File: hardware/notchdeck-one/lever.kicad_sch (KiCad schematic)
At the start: 5 parts, among them U5 AS5600

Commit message: Add schematic wiring notes support
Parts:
- added C14, C15, C16, C17: 100nF, Capacitor_SMD:C_0402_1005Metric, symbol Device:C
- added J5: CODE S0, Connector_JST:JST_PH_S2B-PH-SM4-TB_1x02-1MP_P2.00mm_Horizontal, symbol Connector_Generic:Conn_01x02
- added J6: CODE S1, Connector_JST:JST_PH_S2B-PH-SM4-TB_1x02-1MP_P2.00mm_Horizontal, symbol Connector_Generic:Conn_01x02
- added J7: CODE S2, Connector_JST:JST_PH_S2B-PH-SM4-TB_1x02-1MP_P2.00mm_Horizontal, symbol Connector_Generic:Conn_01x02
- added J8: CODE S3, Connector_JST:JST_PH_S2B-PH-SM4-TB_1x02-1MP_P2.00mm_Horizontal, symbol Connector_Generic:Conn_01x02
- added R14, R15, R16, R17: 10k, Resistor_SMD:R_0402_1005Metric, symbol Device:R
- added R18, R19, R20, R21: 1k, Resistor_SMD:R_0402_1005Metric, symbol Device:R
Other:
- note added: "NotchDeck One — Lever sensing: AS5600 magnetic angle (I2C0) + 4-bit coded-switch input (J5). Placed, not wired. See NETPLAN.md "Lever sensing". AS5600 U5: VDD5V(1) + VDD3V3(2) -> +3V3 (3.3V mode: tie both). GND(4) -> GND. DIR(8) -> GND (CW = increasing). SDA(6) / SCL(7) -> I2C0 bus. OUT(3) = NC, PGO(5) = NC. C11 100nF + C12 1uF decouple. I2C0 (TWIM0): SDA = P0.26 (pad 12), SCL = P0.06 (pad 14). R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"
- note removed: "NotchDeck One — Lever sensor (U5 AS5600, magnetic angle). Placed, not wired. See NETPLAN.md "I2C buses" / "Lever sensing". AS5600 U5: VDD5V(1) + VDD3V3(2) -> +3V3 (3.3V mode: tie both). GND(4) -> GND. DIR(8) -> GND (CW = increasing). SDA(6) / SCL(7) -> I2C0 bus. OUT(3) = NC, PGO(5) = NC. C11 100nF + C12 1uF decouple. I2C0 (TWIM0): SDA = P0.26 (pad 12), SCL = P0.06 (pad 14). R9 / R10 = 4.7k pull-u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"
- title: NotchDeck One — Lever sensor (AS5600, I2C0) -> NotchDeck One — Lever sensing (AS5600 magnetic + 4-bit coded-switch)

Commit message: Wire and verify NotchDeck controller schematics
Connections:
- net at R19.1: now also J6.1 (Pin_1), R15.2
- net LEVER_S1: now reaches R19.2
- net LEVER_S1: now also C15.1
- net +3V3: now reaches R9.1
- net +3V3: now also C11.1, C12.1, R10.1, R14.1, R15.1, R16.1, R17.1, U5.1 (VDD5V), U5.2 (VDD3V3)
- net I2C0_SDA: now reaches R9.2
- net I2C0_SDA: now also U5.6 (SDA)
- net LEVER_S0: now reaches C14.1
- net LEVER_S0: now also R18.2
- net GND: now reaches C14.2
- net GND: now also C11.2, C12.2, C15.2, C16.2, C17.2, J5.2 (Pin_2), J6.2 (Pin_2), J7.2 (Pin_2), J8.2 (Pin_2), U5.4 (GND), U5.8 (DIR)
- net LEVER_S3: now reaches C17.1
- net LEVER_S3: now also R21.2
- net at J5.1 (Pin_1): now also R14.2, R18.1
- net at J8.1 (Pin_1): now also R17.2, R21.1
- net I2C0_SCL: now reaches U5.7 (SCL)
- net I2C0_SCL: now also R10.2
- net at J7.1 (Pin_1): now also R16.2, R20.1
- net LEVER_S2: now reaches C16.1
- net LEVER_S2: now also R20.2
- no-connect marks 0 -> 2
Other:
- note added: "AS5600: 3.3V mode, VDD5V tied to VDD3V3. I2C0 / 0x36; separate from the fuel gauge. DIR = GND, clockwise increases angle. OUT and PGO intentionally unused."
- note added: "J5-J8: pin 1 = switch signal, pin 2 = GND. Both sensing front-ends may be populated. RC release ~1.1ms, press ~0.1ms. Firmware still debounces and decodes binary/Gray detent codes."
- note added: "S0: switch closes to GND. 10k pull-up / 1k series / 100nF."
- note added: "S1: switch closes to GND. 10k pull-up / 1k series / 100nF."
- note added: "S2: switch closes to GND. 10k pull-up / 1k series / 100nF."
- note added: "S3: switch closes to GND. 10k pull-up / 1k series / 100nF."
- note removed: "NotchDeck One — Lever sensing: AS5600 magnetic angle (I2C0) + 4-bit coded-switch input (J5). Placed, not wired. See NETPLAN.md "Lever sensing". AS5600 U5: VDD5V(1) + VDD3V3(2) -> +3V3 (3.3V mode: tie both). GND(4) -> GND. DIR(8) -> GND (CW = increasing). SDA(6) / SCL(7) -> I2C0 bus. OUT(3) = NC, PGO(5) = NC. C11 100nF + C12 1uF decouple. I2C0 (TWIM0): SDA = P0.26 (pad 12), SCL = P0.06 (pad 14). R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"
- title: NotchDeck One — Lever sensing (AS5600 magnetic + 4-bit coded-switch) -> NotchDeck One — Lever sensing

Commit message: Source controller BOM from JLCPCB and align selected footprints
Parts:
- C11, C14, C15, C16, C17: BOM Checked (none) -> 2026-10-03; BOM Comments (none) -> 100nF 16V X7R ±10% 0402 Multilayer Ceramic Capacitors MLCC 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; JLCPCB Part Type (none) -> Basic; LCSC (none) -> C1525; MPN (none) -> CL05B104KO5NNNC; Manufacturer (none) -> Samsung Electro-Mechanics
- C12: BOM Checked (none) -> 2026-10-03; BOM Comments (none) -> 1uF 25V X5R ±10% 0402 Multilayer Ceramic Capacitors MLCC - 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; JLCPCB Part Type (none) -> Basic; LCSC (none) -> C52923; MPN (none) -> CL05A105KA5NQNC; Manufacturer (none) -> Samsung Electro-Mechanics
- J5, J6, J7, J8: BOM Checked (none) -> 2026-10-03; BOM Comments (none) -> Mating harnesses not included. J2: protected 1S cell, pin 1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; JLCPCB Part Type (none) -> Extended; LCSC (none) -> C295747; MPN S2B-PH-SM4-TB -> S2B-PH-SM4-TB(LF)(SN)
- R10, R9: BOM Checked (none) -> 2026-10-03; BOM Comments (none) -> -55℃~+155℃ 4.7kΩ 50V 62.5mW Thick Film Resistor ±1% ±100ppm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; JLCPCB Part Type (none) -> Basic; LCSC (none) -> C25900; MPN (none) -> 0402WGF4701TCE; Manufacturer (none) -> UNI-ROYAL
- R14, R15, R16, R17: BOM Checked (none) -> 2026-10-03; BOM Comments (none) -> -55℃~+155℃ 10kΩ 50V 62.5mW Thick Film Resistor ±1% ±100ppm/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; JLCPCB Part Type (none) -> Basic; LCSC (none) -> C25744; MPN (none) -> 0402WGF1002TCE; Manufacturer (none) -> UNI-ROYAL
- R18, R19, R20, R21: BOM Checked (none) -> 2026-10-03; BOM Comments (none) -> -55℃~+155℃ 1kΩ 50V 62.5mW Thick Film Resistor ±1% ±100ppm/℃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; JLCPCB Part Type (none) -> Basic; LCSC (none) -> C11702; MPN (none) -> 0402WGF1001TCE; Manufacturer (none) -> UNI-ROYAL
- U5: BOM Checked (none) -> 2026-10-03; JLCPCB Part Type (none) -> Extended; MPN AS5600-ASOM -> AS5600-ASOT; Manufacturer AMS -> ams

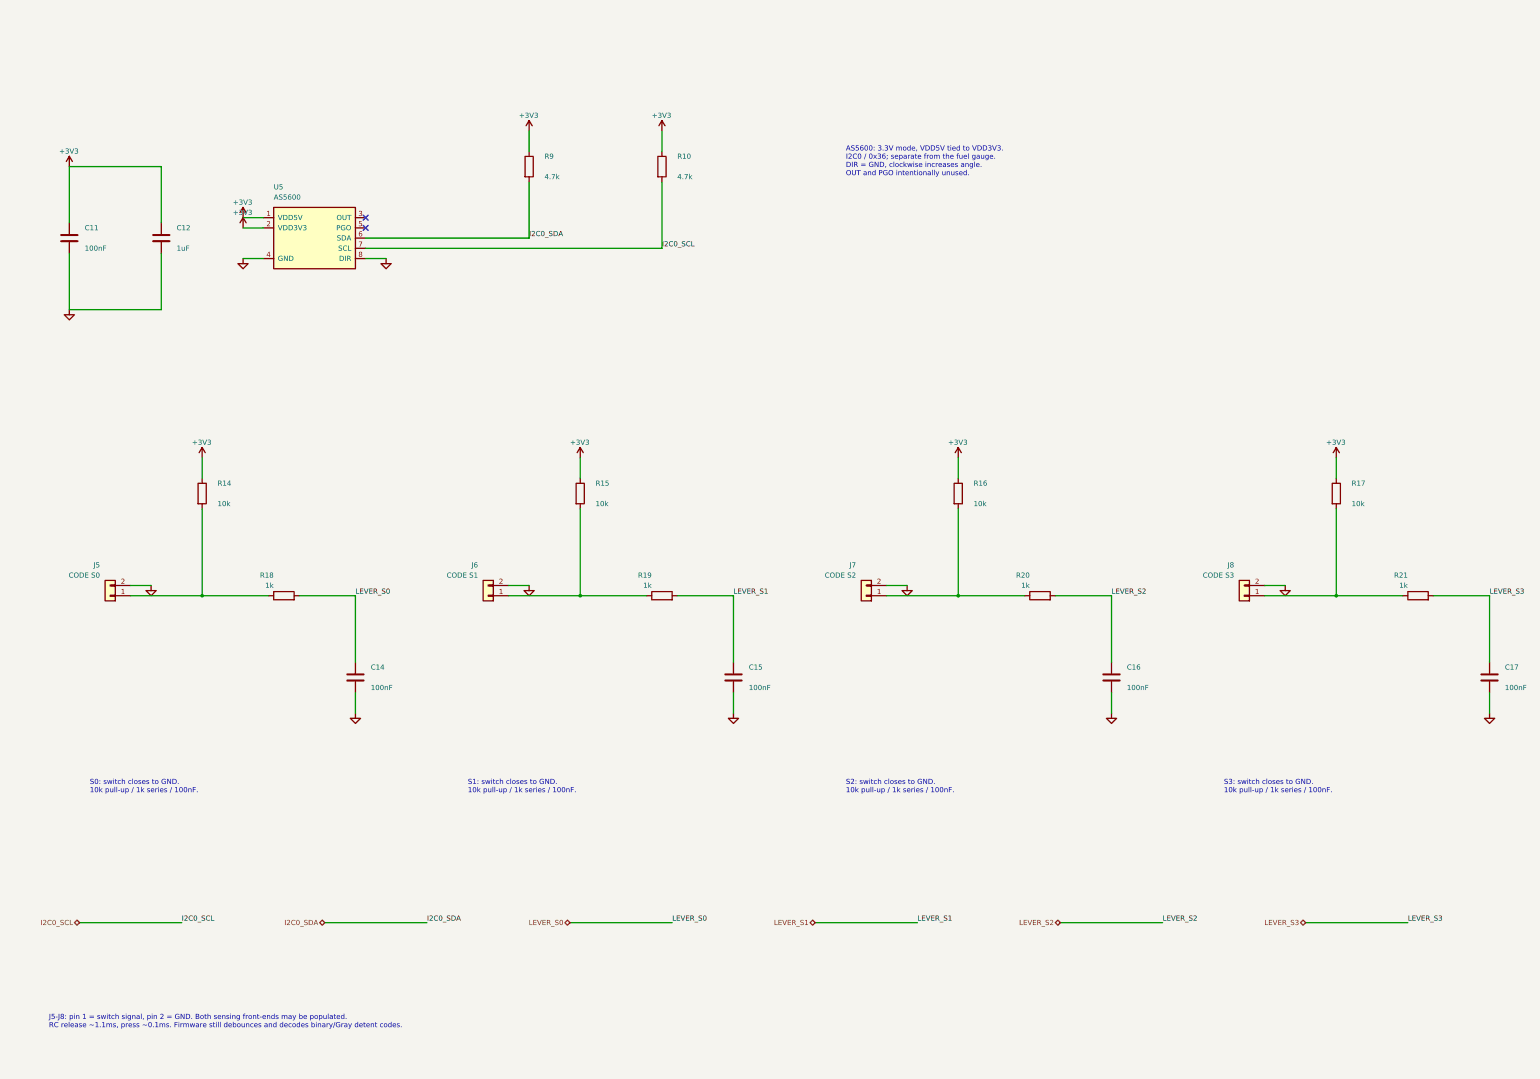
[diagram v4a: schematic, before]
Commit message: Support independent magnetic and Gray-coded power and brake handles
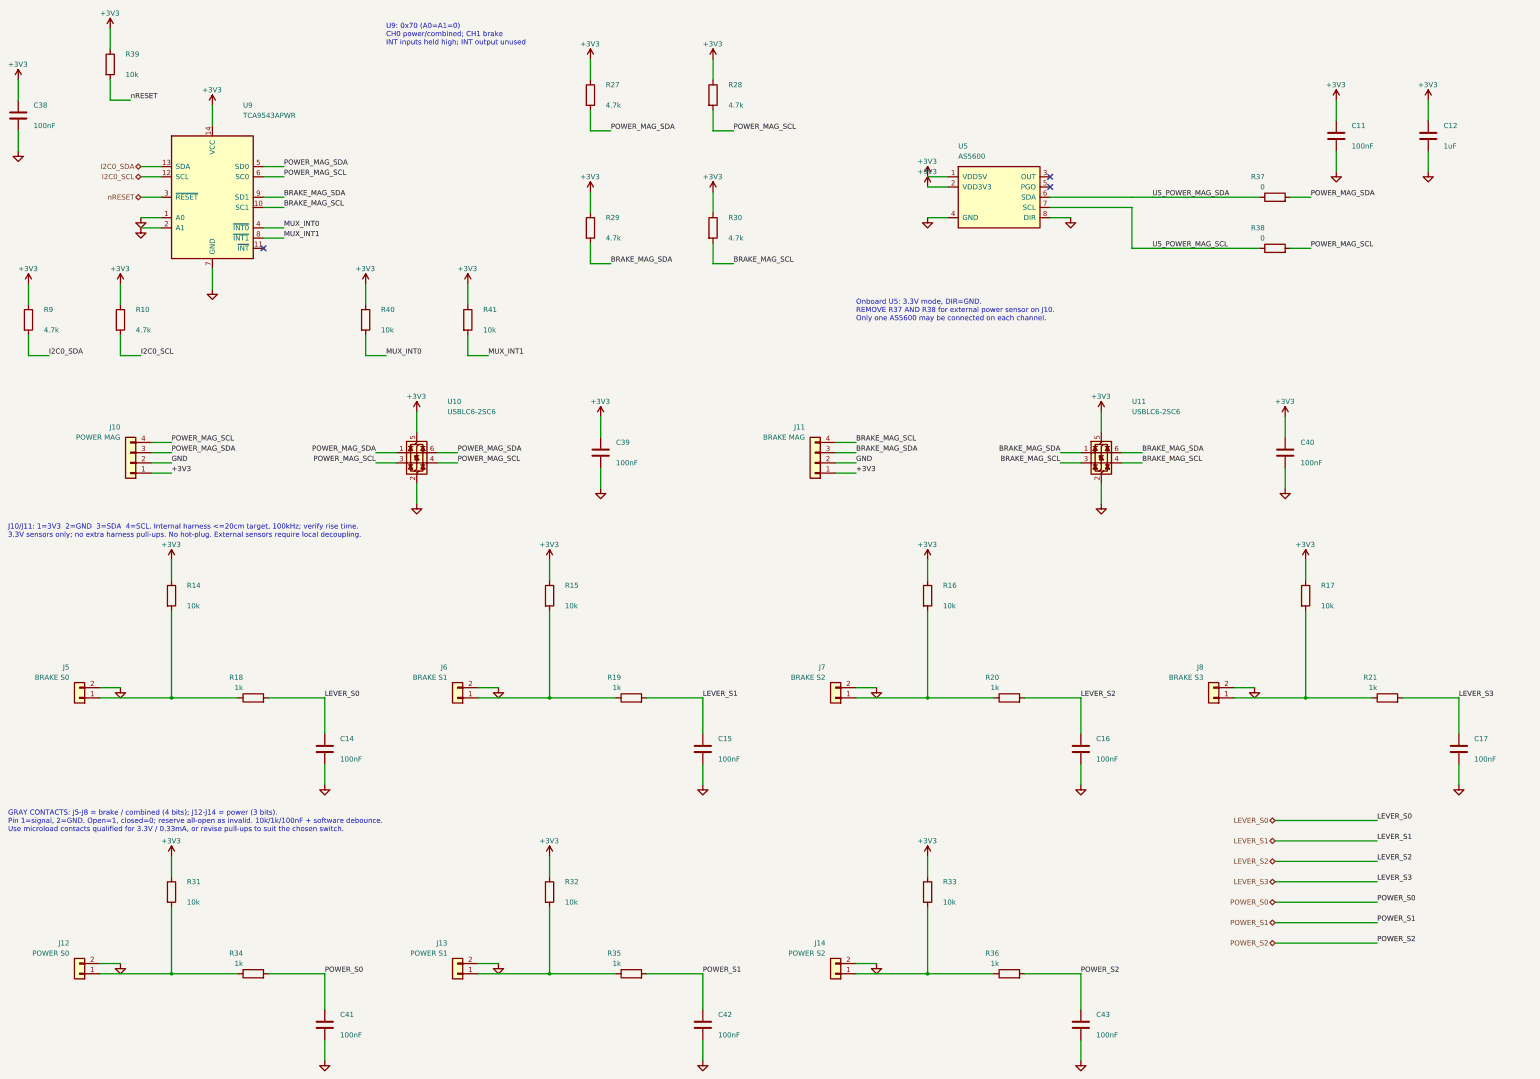
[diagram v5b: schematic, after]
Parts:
- added C38, C39, C40, C41, C42, C43: 100nF, Capacitor_SMD:C_0402_1005Metric, symbol Device:C
- added J10: POWER MAG, Connector_JST:JST_PH_S4B-PH-SM4-TB_1x04-1MP_P2.00mm_Horizontal, symbol Connector_Generic:Conn_01x04
- added J11: BRAKE MAG, Connector_JST:JST_PH_S4B-PH-SM4-TB_1x04-1MP_P2.00mm_Horizontal, symbol Connector_Generic:Conn_01x04
- added J12: POWER S0, Connector_JST:JST_PH_S2B-PH-SM4-TB_1x02-1MP_P2.00mm_Horizontal, symbol Connector_Generic:Conn_01x02
- added J13: POWER S1, Connector_JST:JST_PH_S2B-PH-SM4-TB_1x02-1MP_P2.00mm_Horizontal, symbol Connector_Generic:Conn_01x02
- added J14: POWER S2, Connector_JST:JST_PH_S2B-PH-SM4-TB_1x02-1MP_P2.00mm_Horizontal, symbol Connector_Generic:Conn_01x02
- added R27, R28, R29, R30: 4.7k, Resistor_SMD:R_0402_1005Metric, symbol Device:R
- added R31, R32, R33, R39, R40, R41: 10k, Resistor_SMD:R_0402_1005Metric, symbol Device:R
- added R34, R35, R36: 1k, Resistor_SMD:R_0402_1005Metric, symbol Device:R
- added R37, R38: 0, Resistor_SMD:R_0603_1608Metric, symbol Device:R
- added U10, U11: USBLC6-2SC6, Package_TO_SOT_SMD:SOT-23-6, symbol Power_Protection:USBLC6-2SC6
- added U9: TCA9543APWR, Package_SO:TSSOP-14_4.4x5mm_P0.65mm, symbol notchdeck:TCA9543APWR
- J5: value CODE S0 -> BRAKE S0
- J6: value CODE S1 -> BRAKE S1
- J7: value CODE S2 -> BRAKE S2
- J8: value CODE S3 -> BRAKE S3
- U5: BOM Comments (none) -> Onboard power/combined magnetic sensor. Remove R37/R38 for 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
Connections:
- net +3V3: now also C38.1, C39.1, C40.1, J10.1 (Pin_1), J11.1 (Pin_1), R27.1, R28.1, R29.1, R30.1, R31.1, R32.1, R33.1, R39.1, R40.1, R41.1, U10.5 (VBUS), U11.5 (VBUS), U9.14 (VCC)
- net GND: now also C38.2, C39.2, C40.2, C41.2, C42.2, C43.2, J10.2 (Pin_2), J11.2 (Pin_2), J12.2 (Pin_2), J13.2 (Pin_2), J14.2 (Pin_2), U10.2 (GND), U11.2 (GND), U9.1 (A0), U9.2 (A1), U9.7 (GND)
- net I2C0_SCL: now also U9.12 (SCL); no longer U5.7 (SCL)
- net I2C0_SDA: now also U9.13 (SDA); no longer U5.6 (SDA)
- new net: J12.1 (Pin_1), R31.2, R34.1
- new net: J13.1 (Pin_1), R32.2, R35.1
- new net: J14.1 (Pin_1), R33.2, R36.1
- new net BRAKE_MAG_SCL: J11.4 (Pin_4), R30.2, U11.3 (I/O2), U11.4 (I/O2), U9.10 (SC1)
- new net BRAKE_MAG_SDA: J11.3 (Pin_3), R29.2, U11.1 (I/O1), U11.6 (I/O1), U9.9 (SD1)
- new net MUX_INT0: R40.2, U9.4 (~{INT0})
- new net MUX_INT1: R41.2, U9.8 (~{INT1})
- new net POWER_MAG_SCL: J10.4 (Pin_4), R28.2, R38.2, U10.3 (I/O2), U10.4 (I/O2), U9.6 (SC0)
- new net POWER_MAG_SDA: J10.3 (Pin_3), R27.2, R37.2, U10.1 (I/O1), U10.6 (I/O1), U9.5 (SD0)
- new net POWER_S0: C41.1, R34.2
- new net POWER_S1: C42.1, R35.2
- new net POWER_S2: C43.1, R36.2
- new net U5_POWER_MAG_SCL: R38.1, U5.7 (SCL)
- new net U5_POWER_MAG_SDA: R37.1, U5.6 (SDA)
- new net nRESET: R39.2, U9.3 (~{RESET})
- no-connect marks 2 -> 3
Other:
- note added: "GRAY CONTACTS: J5-J8 = brake / combined (4 bits); J12-J14 = power (3 bits). Pin 1=signal, 2=GND. Open=1, closed=0; reserve all-open as invalid. 10k/1k/100nF + software debounce. Use microload contacts qualified for 3.3V / 0.33mA, or revise pull-ups to suit the chosen switch."
- note added: "J10/J11: 1=3V3 2=GND 3=SDA 4=SCL. Internal harness <=20cm target, 100kHz; verify rise time. 3.3V sensors only; no extra harness pull-ups. No hot-plug. External sensors require local decoupling."
- note added: "Onboard U5: 3.3V mode, DIR=GND. REMOVE R37 AND R38 for external power sensor on J10. Only one AS5600 may be connected on each channel."
- note added: "U9: 0x70 (A0=A1=0) CH0 power/combined; CH1 brake INT inputs held high; INT output unused"
- note removed: "AS5600: 3.3V mode, VDD5V tied to VDD3V3. I2C0 / 0x36; separate from the fuel gauge. DIR = GND, clockwise increases angle. OUT and PGO intentionally unused."
- note removed: "J5-J8: pin 1 = switch signal, pin 2 = GND. Both sensing front-ends may be populated. RC release ~1.1ms, press ~0.1ms. Firmware still debounces and decodes binary/Gray detent codes."
- note removed: "S0: switch closes to GND. 10k pull-up / 1k series / 100nF."
- note removed: "S1: switch closes to GND. 10k pull-up / 1k series / 100nF."
- note removed: "S2: switch closes to GND. 10k pull-up / 1k series / 100nF."
- note removed: "S3: switch closes to GND. 10k pull-up / 1k series / 100nF."
- title: NotchDeck One — Lever sensing -> NotchDeck One — Power and brake handle interfaces
- moved on the sheet: C11, C12, C14, C15, C16, C17, J5, J6, J7, J8, R10, R14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
